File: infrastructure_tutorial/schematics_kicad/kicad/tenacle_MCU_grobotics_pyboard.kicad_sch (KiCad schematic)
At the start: 3 parts, among them T301 tentacle_octobus, T302 tentacle_relay

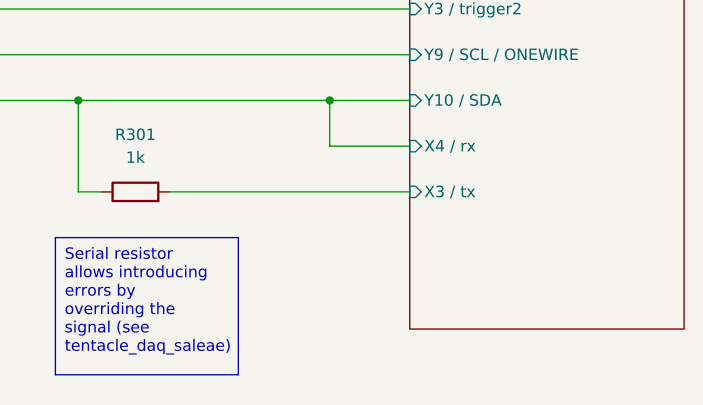
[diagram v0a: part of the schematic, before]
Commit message: Connect pyboard/pico to ground
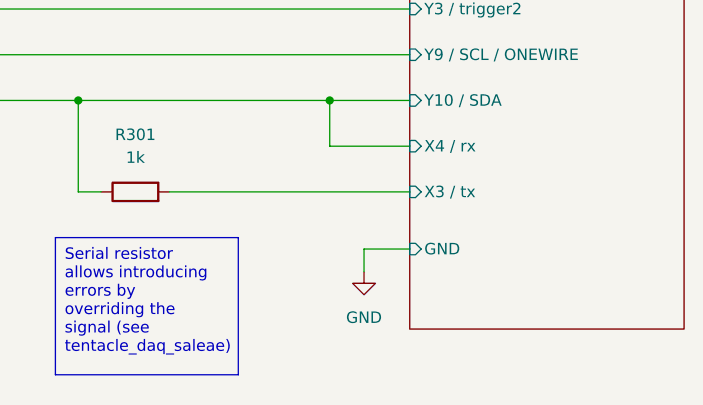
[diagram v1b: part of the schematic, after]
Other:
- sheet pyboard3 ports: added GND; removed none
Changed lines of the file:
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@@
+	(wire
+		(pts
+			(xy 179.07 91.44) (xy 173.99 91.44)
+		)
+		(stroke
+			(width 0)
+			(type default)
+		)
+	)
 	(wire
 		(pts
@@
 		(pts
 			(xy 74.93 64.77) (xy 104.14 64.77)
+		)
+		(stroke
+			(width 0)
+			(type default)
+		)
+	)
+	(wire
+		(pts
+			(xy 173.99 91.44) (xy 173.99 93.98)
 		)
 		(stroke
@@
 	(symbol
 		(lib_id "power:GND")
+		(at 173.99 93.98 0)
+		(unit 1)
+		(exclude_from_sim no)
+		(in_bom yes)
+		(on_board yes)
+		(dnp no)
+		(fields_autoplaced yes)
+		(property "Reference" "#PWR0303"
+			(at 173.99 100.33 0)
+			(effects
+				(font
+					(size 1.27 1.27)
+				)
+				(hide yes)
+			)
+		)
+		(property "Value" "GND"
+			(at 173.99 99.06 0)
+			(effects
+				(font
+					(size 1.27 1.27)
+				)
+			)
+		)
+		(property "Footprint" ""
+			(at 173.99 93.98 0)
+			(effects
+				(font
+					(size 1.27 1.27)
+				)
+				(hide yes)
+			)
+		)
+		(property "Datasheet" ""
+			(at 173.99 93.98 0)
+			(effects
+				(font
+					(size 1.27 1.27)
+				)
+				(hide yes)
+			)
+		)
+		(property "Description" "Power symbol creates a global label with name \"GND\" , ground"
+			(at 173.99 93.98 0)
+			(effects
+				(font
+					(size 1.27 1.27)
+				)
+				(hide yes)
+			)
+		)
+		(pin "1"
+		)
+		(instances
+			(project "infrastructure"
+				(path "/188054c4-74b7-429a-b3f5-c6f3151e27de/a196d1ad-2a7e-47a3-8a53-65ea8ad08c90"
+					(reference "#PWR0303")
+					(unit 1)
+				)
+			)
+		)
+	)
+	(symbol
+		(lib_id "power:GND")
 		(at 48.26 100.33 0)
 		(unit 1)
@@
 			(effects
 				(font
+					(size 1.27 1.27)
+				)
+				(justify left)
+			)
+		)
+		(pin "GND" input
+			(at 179.07 91.44 180)
+			(effects
+				(font
